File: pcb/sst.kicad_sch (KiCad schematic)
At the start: 36 parts, among them X1 CONN_SPI, X2 CONN_PWR, X3 CONN_INPUTS, X4 CONN_I2C, X5 CONN_INPUTS

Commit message: доработка принципиальной схемы: VD3 без ворнинга
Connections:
- net +2V5: now also VD3.1 (K); no longer VD3. (K)
- net GND: now also VD3.2 (A); no longer VD3. (K)
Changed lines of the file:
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@@
 			)
 		)
-		(pin ""
+		(pin "2"
 		)
-		(pin ""
+		(pin "1"
 		)
 		(instances

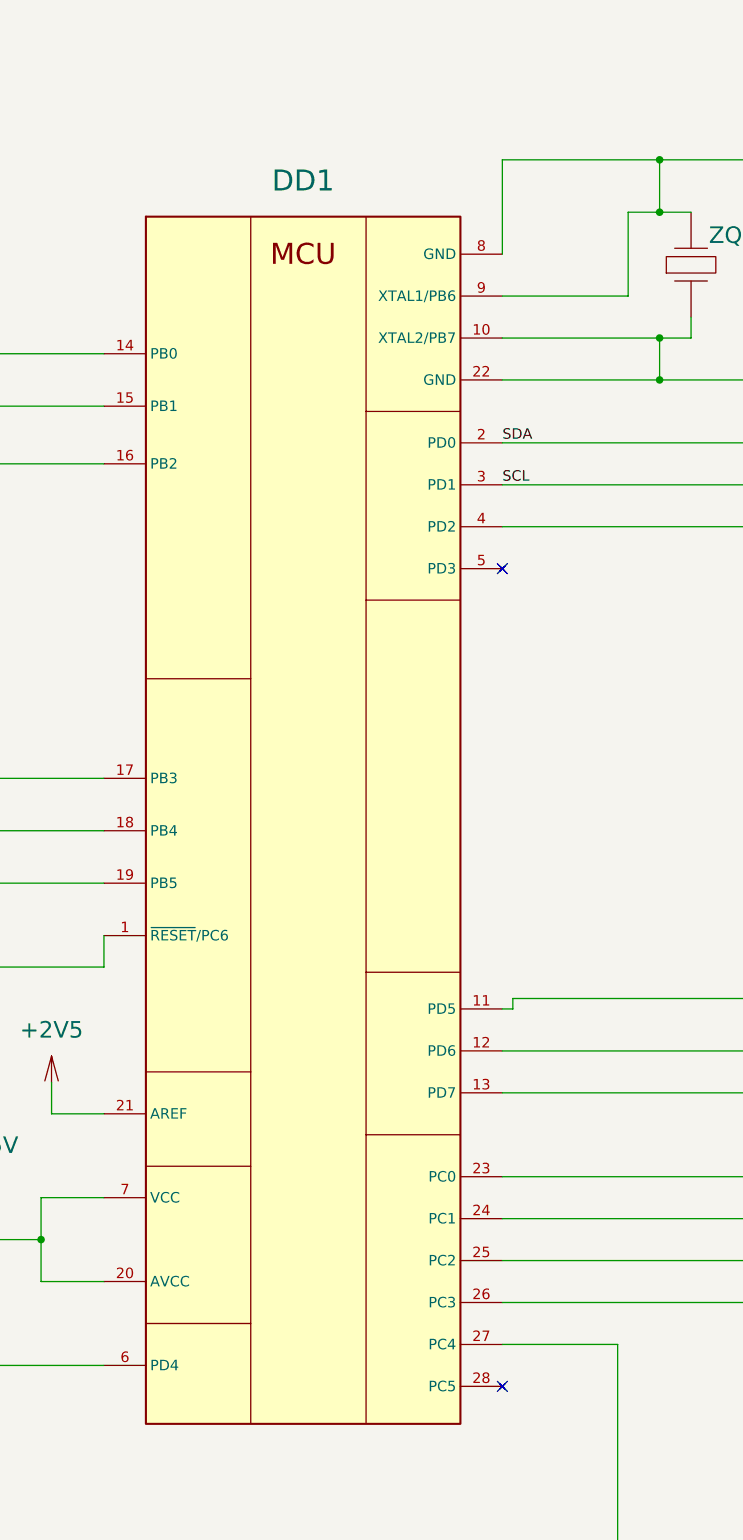
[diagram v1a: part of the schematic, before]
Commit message: доработка схемы до требований Алексеева
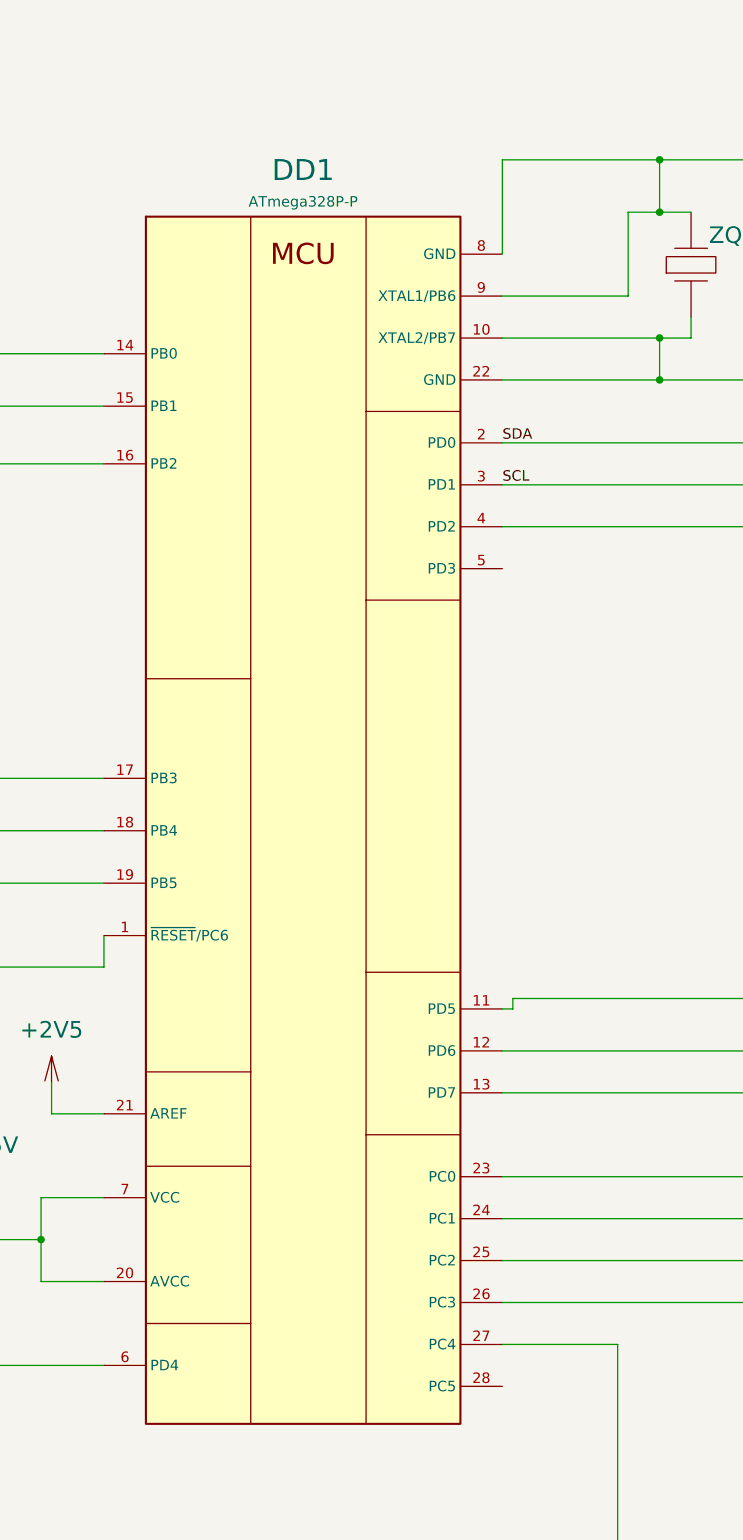
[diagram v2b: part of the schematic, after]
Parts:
- DD1: value Микроконтроллер ATmega328P -> ATmega328P-P
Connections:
- no-connect marks 5 -> 3
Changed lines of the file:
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@@
 	)
 	(no_connect
-		(at 243.84 110.49)
-	)
-	(no_connect
-		(at 243.84 209.55)
-	)
-	(no_connect
 		(at 67.31 334.645)
 	)
@@
 		(fields_autoplaced yes)
 		(property "Reference" "DD1"
-			(at 219.71 63.5 0)
+			(at 219.71 62.23 0)
 			(effects
 				(font
@@
 			)
 		)
-		(property "Value" "Микроконтроллер ATmega328P"
+		(property "Value" "ATmega328P-P"
 			(at 219.71 66.04 0)
 			(effects
@@
 					(size 1.27 1.27)
 				)
-				(hide yes)
 			)
 		)

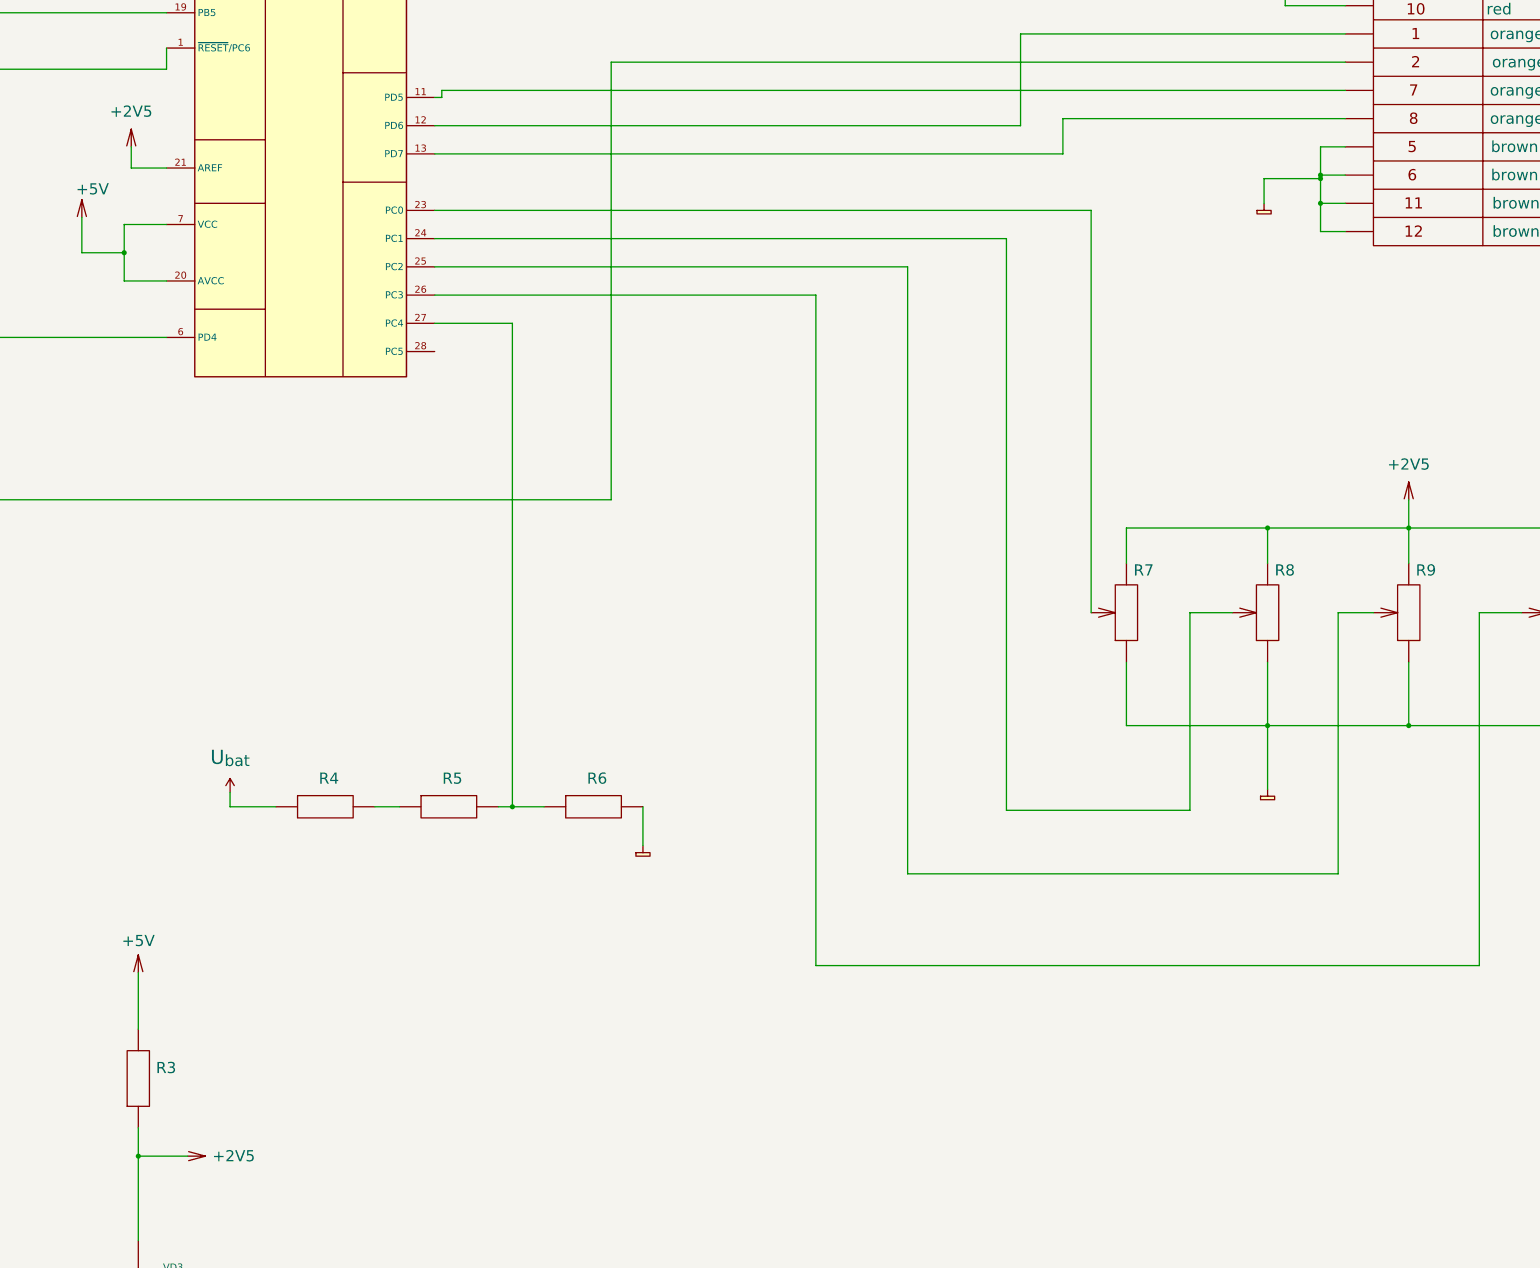
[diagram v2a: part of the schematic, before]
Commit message: Обозначение питания как +2,5V, а не 2V5
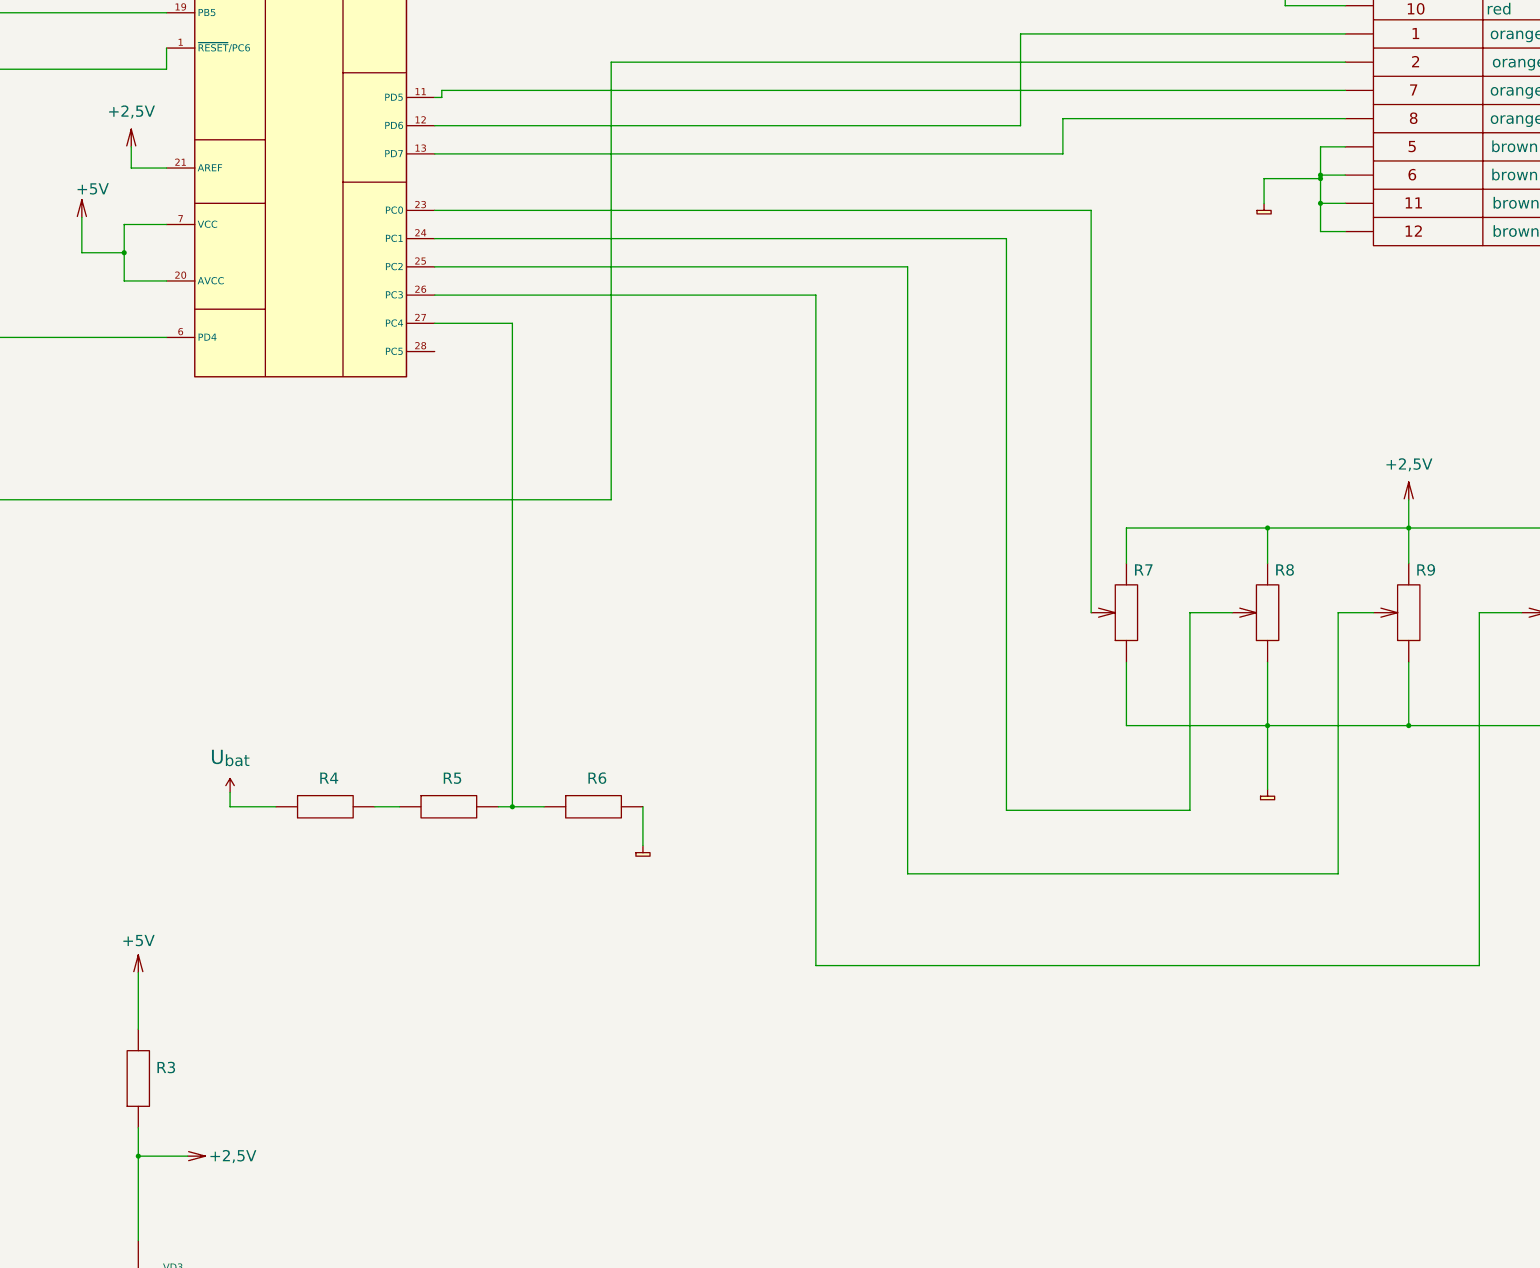
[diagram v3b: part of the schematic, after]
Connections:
- net +2V5 renamed +2,5V
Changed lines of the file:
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@@
 		(dnp no)
 		(fields_autoplaced yes)
-		(property "Reference" "#PWR016"
+		(property "Reference" "#PWR16"
 			(at 196.85 354.33 0)
 			(effects
@@
 			)
 		)
-		(property "Value" "+2V5"
-			(at 203.835 354.33 90)
+		(property "Value" "+2,5V"
+			(at 203.2 354.33 90)
 			(effects
 				(font
@@
 			(project ""
 				(path "/d486a0a8-b0b2-426a-9635-bf463f56fa2d"
-					(reference "#PWR016")
+					(reference "#PWR16")
 					(unit 1)
 				)
@@
 		(dnp no)
 		(fields_autoplaced yes)
-		(property "Reference" "#PWR013"
+		(property "Reference" "#PWR13"
 			(at 189.23 175.26 0)
 			(effects
@@
 			)
 		)
-		(property "Value" "+2V5"
+		(property "Value" "+2,5V"
 			(at 189.23 166.37 0)
 			(effects
@@
 			(project ""
 				(path "/d486a0a8-b0b2-426a-9635-bf463f56fa2d"
-					(reference "#PWR013")
+					(reference "#PWR13")
 					(unit 1)
 				)
@@
 		(dnp no)
 		(fields_autoplaced yes)
-		(property "Reference" "#PWR023"
+		(property "Reference" "#PWR23"
 			(at 419.1 238.76 0)
 			(effects
@@
 			)
 		)
-		(property "Value" "+2V5"
+		(property "Value" "+2,5V"
 			(at 419.1 229.87 0)
 			(effects
@@
 			(project ""
 				(path "/d486a0a8-b0b2-426a-9635-bf463f56fa2d"
-					(reference "#PWR023")
-					(unit 1)
-				)
+					(reference "#PWR23")
+					(unit 1)
+				)

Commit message: заполнил новый перечень резисторами
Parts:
- R3: footprint Resistor_THT:R_Axial_DIN0204_L3.6mm_D1.6mm_P5.08mm_Horizontal -> Resistor_THT:R_Axial_DIN0207_L6.3mm_D2.5mm_P7.62mm_Horizontal
- R7: value 10к 0,25Вт -> потенциометр 10к 0,25Вт
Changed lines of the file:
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@@
 			)
 		)
-		(property "Value" "10к 0,25Вт"
+		(property "Value" "потенциометр 10к 0,25Вт"
 			(at 372.11 254 90)
 			(effects
@@
 		(dnp no)
 		(property "Reference" "X5"
-			(at 446.532 117.348 0)
+			(at 432.816 119.634 0)
 			(effects
 				(font
@@
 			)
 		)
-		(property "Footprint" "Resistor_THT:R_Axial_DIN0204_L3.6mm_D1.6mm_P5.08mm_Horizontal"
+		(property "Footprint" "Resistor_THT:R_Axial_DIN0207_L6.3mm_D2.5mm_P7.62mm_Horizontal"
 			(at 189.865 342.9 0)
 			(effects

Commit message: Значения диодов на схеме
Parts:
- VD1: value VD_Schottky -> 1N5817 шотки
- VD2: value VD_Schottky -> 5,1В шотки
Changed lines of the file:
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@@
 			)
 		)
-		(property "Value" "VD_Schottky"
+		(property "Value" "1N5817  шотки"
 			(at 60.96 248.92 0)
 			(effects
@@
 			)
 		)
-		(property "Value" "VD_Schottky"
+		(property "Value" "5,1В шотки"
 			(at 135.89 372.11 0)
 			(effects

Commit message: выполняя расчёт экономики, обнаружил неточности в перечне
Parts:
- R13: value резистор 22 0,25Вт -> 22 0,25Вт
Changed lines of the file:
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@@
 			)
 		)
-		(property "Value" "резистор 22 0,25Вт"
+		(property "Value" "22 0,25Вт"
 			(at 505.46 177.8 0)
 			(effects

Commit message: перечень элементов, объеденил компоненты
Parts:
- R14: value 10к -> 10к 0,25Вт; footprint Resistor_THT:R_Axial_DIN0204_L3.6mm_D1.6mm_P5.08mm_Horizontal -> Resistor_THT:R_Axial_DIN0207_L6.3mm_D2.5mm_P7.62mm_Horizontal
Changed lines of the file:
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@@
 			)
 		)
-		(property "Value" "10к"
+		(property "Value" "10к 0,25Вт"
 			(at 526.415 198.12 90)
 			(effects
@@
 			)
 		)
-		(property "Footprint" "Resistor_THT:R_Axial_DIN0204_L3.6mm_D1.6mm_P5.08mm_Horizontal"
+		(property "Footprint" "Resistor_THT:R_Axial_DIN0207_L6.3mm_D2.5mm_P7.62mm_Horizontal"
 			(at 522.605 203.2 0)
 			(effects

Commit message: все конденсаторы для экономического обоснования, кондёры на схеме
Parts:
- C4, C5: footprint Capacitor_THT:C_Radial_D6.3mm_H7.0mm_P2.50mm -> Capacitor_SMD:C_0805_2012Metric_Pad1.18x1.45mm_HandSolder
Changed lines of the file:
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@@
 			)
 		)
-		(property "Footprint" "Capacitor_THT:C_Radial_D6.3mm_H7.0mm_P2.50mm"
+		(property "Footprint" "Capacitor_SMD:C_0805_2012Metric_Pad1.18x1.45mm_HandSolder"
 			(at 285.75 85.725 0)
 			(effects
@@
 			)
 		)
-		(property "Footprint" "Capacitor_THT:C_Radial_D6.3mm_H7.0mm_P2.50mm"
+		(property "Footprint" "Capacitor_SMD:C_0805_2012Metric_Pad1.18x1.45mm_HandSolder"
 			(at 285.75 62.865 0)
 			(effects
